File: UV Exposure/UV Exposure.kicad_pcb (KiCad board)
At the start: 2 copper layers, 90 x 90 mm, 90 parts

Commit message: PCB rearrange
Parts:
- moved D37 18.0 mm to (264.2, 38.1)
- moved D38 18.0 mm to (264.2, 50.5)
- moved D39 18.0 mm to (264.2, 63.5)
- moved D40 18.0 mm to (264.2, 76.2)
- moved D41 18.0 mm to (264.2, 88.9)
- moved D42 18.0 mm to (264.2, 101.6)
- moved D31 15.5 mm to (251.5, 38.1)
- moved D32 15.5 mm to (251.5, 50.8)
- moved D33 15.5 mm to (251.5, 63.5)
- moved D36 15.5 mm to (251.5, 101.6)
- moved D34 15.5 mm to (251.5, 76.2)
- moved D35 15.5 mm to (251.5, 88.9)
- moved D26 13.0 mm to (238.8, 50.8)
- moved D27 13.0 mm to (238.8, 63.5)
- moved D30 13.0 mm to (238.8, 101.6)
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
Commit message: Reposition SMD Resistor
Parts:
- moved R35 185.6 mm to (314.9, 108.4)
- moved R33 167.0 mm to (299.9, 108.4)
- moved R36 165.0 mm to (314.9, 111.0)
- moved R26 162.6 mm to (258.0, 111.1)
- moved R34 156.5 mm to (300.0, 111.0)
- moved R32 147.3 mm to (275.1, 111.0)
- moved R15 138.5 mm to (229.3, 108.4)
- moved R31 135.6 mm to (275.1, 108.4)
- moved R30 129.0 mm to (269.7, 111.0)
- moved R28 127.6 mm to (264.2, 111.0)
- moved R29 125.4 mm to (269.7, 108.4)
- moved R27 125.3 mm to (264.2, 108.4)
- moved R25 124.6 mm to (258.0, 108.4)
- moved R19 121.7 mm to (240.7, 108.4)
- moved R4 118.1 mm to (193.8, 111.0)
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
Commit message: Rearrange components
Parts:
- moved D43 165.2 mm to (134.6, 38.1)
- moved D44 165.2 mm to (134.6, 50.8)
- moved D45 165.2 mm to (134.6, 63.5)
- moved D46 165.2 mm to (134.6, 76.2)
- moved D47 165.2 mm to (134.6, 88.9)
- moved D48 165.2 mm to (134.6, 101.6)
- moved D37 142.3 mm to (121.9, 38.1)
- moved D38 142.3 mm to (121.9, 50.5)
- moved D39 142.3 mm to (121.9, 63.5)
- moved D40 142.3 mm to (121.9, 76.2)
- moved D41 142.3 mm to (121.9, 88.9)
- moved D42 142.3 mm to (121.9, 101.6)
- moved D1 142.3 mm to (45.7, 38.1)
- moved D2 142.3 mm to (45.7, 50.8)
- moved D3 142.3 mm to (45.7, 63.5)
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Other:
- board size 90 x 90 mm -> 102 x 90 mm

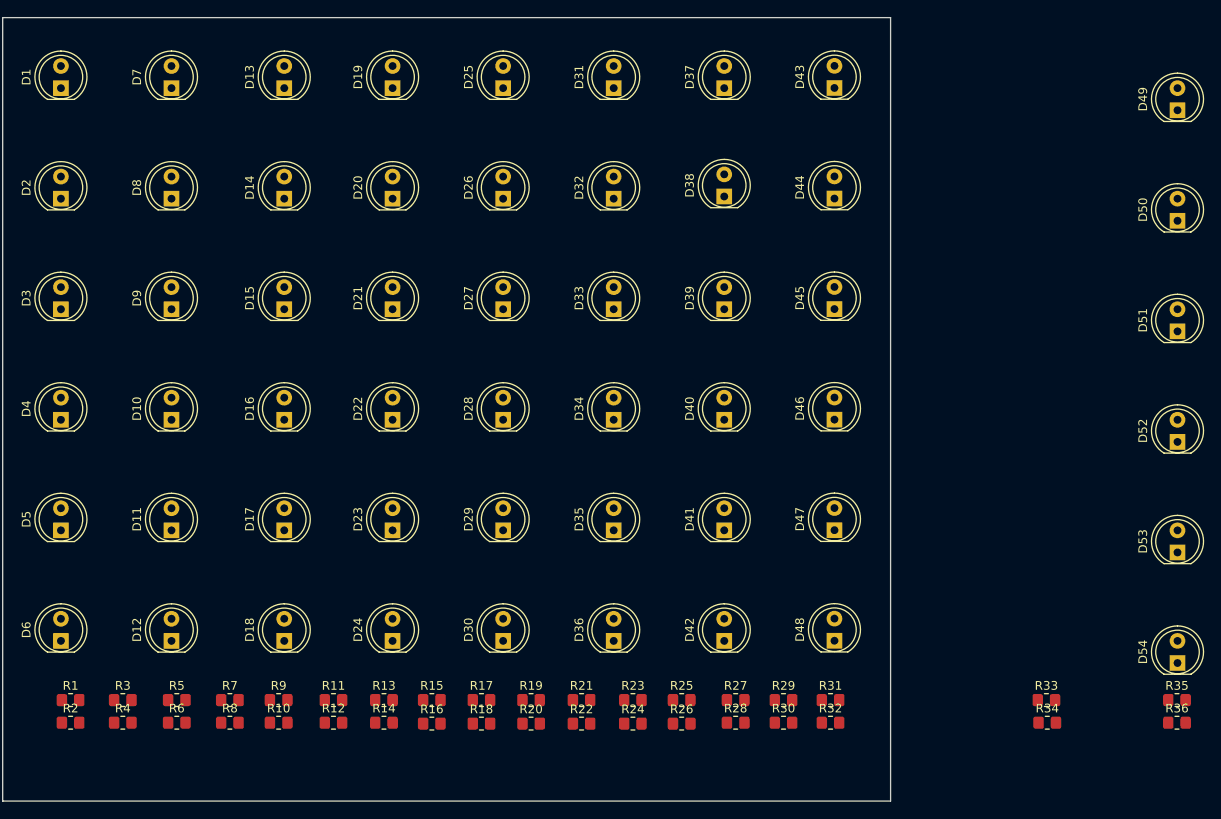
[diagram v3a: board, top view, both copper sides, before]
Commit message: drawing pcb track
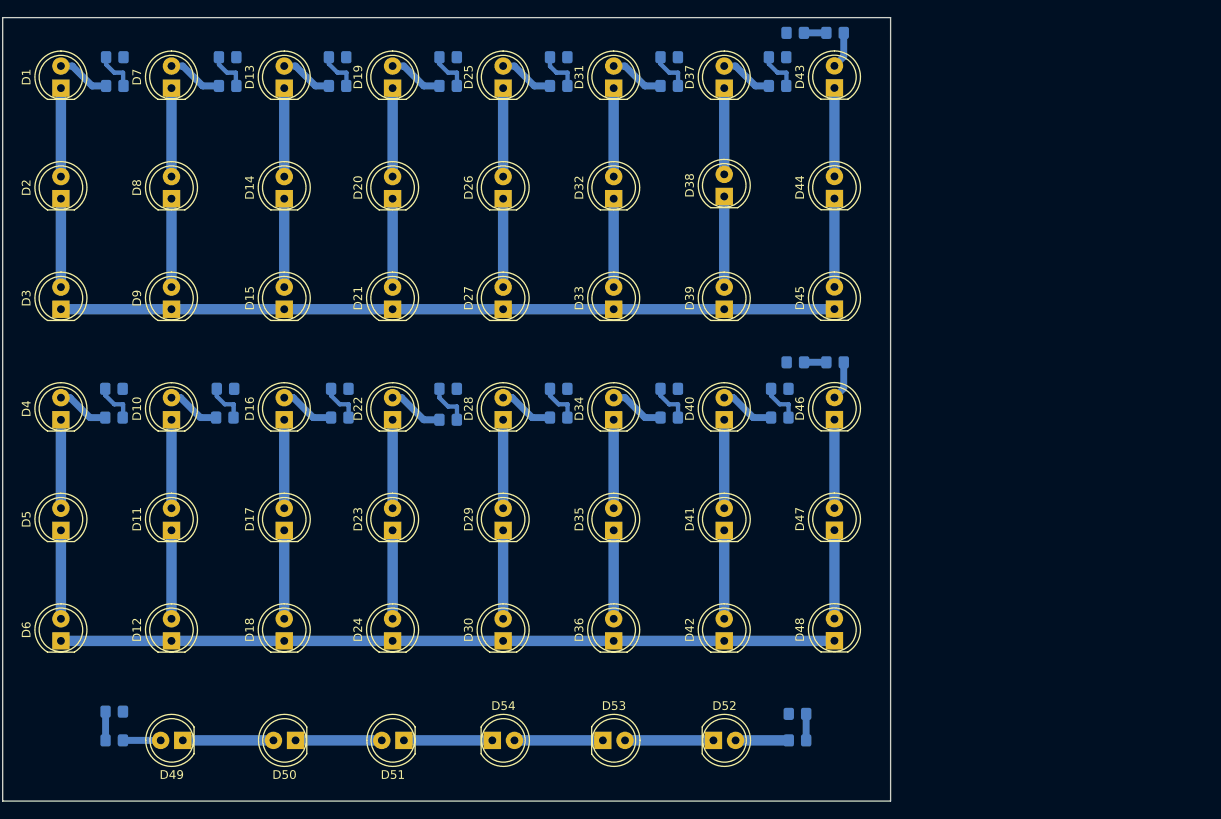
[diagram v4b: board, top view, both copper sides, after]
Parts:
- R1, R10, R11, R12, R13, R14, R15, R16, R17, R18, R19, R2, R20, R21, R22, R23, R24, R25, R26, R27, R28, R29, R3, R30, R31, R32, R33, R34, R35, R36, R4, R5, R6, R7, R8, R9: moved to B.Cu
- moved D49 135.3 mm to (59.7, 113.0), turned to 180 degrees
- moved D50 117.6 mm to (72.6, 113.0), turned to 180 degrees
- moved R34 107.2 mm to (51.8, 113.0), turned to 180 degrees
- moved R33 107.1 mm to (51.8, 109.7)
- moved D51 100.5 mm to (85.1, 113.0), turned to 180 degrees
- moved R30 79.5 mm to (134.6, 31.8), turned to 180 degrees
- moved D54 79.2 mm to (95.2, 113.0), turned to 0 degrees
- moved R29 76.7 mm to (130.0, 31.8), turned to 180 degrees
- moved R25 74.7 mm to (128.0, 34.5)
- moved R21 74.5 mm to (115.6, 34.5)
- moved R17 74.4 mm to (102.9, 34.5)
- moved R13 74.2 mm to (90.2, 34.5)
- moved R9 74.2 mm to (77.5, 34.5)
- moved R5 74.1 mm to (64.8, 34.5)
- moved R26 74.1 mm to (128.0, 37.8)
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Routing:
- net GND: track 0.00 -> 188.2 mm
- net Net-(D49-Pad1): track 0.00 -> 10.4 mm
- net Net-(D38-Pad1): track 0.00 -> 10.4 mm
- net Net-(D52-Pad1): track 0.00 -> 10.2 mm
- net Net-(D8-Pad1): track 0.00 -> 10.2 mm
- net Net-(D44-Pad1): track 0.00 -> 10.2 mm
- net Net-(D32-Pad1): track 0.00 -> 10.2 mm
- net Net-(D26-Pad1): track 0.00 -> 10.2 mm
- net Net-(D20-Pad1): track 0.00 -> 10.2 mm
- net Net-(D2-Pad1): track 0.00 -> 10.2 mm
- net Net-(D14-Pad1): track 0.00 -> 10.2 mm
- net Net-(D7-Pad1): track 0.00 -> 10.2 mm
- net Net-(D53-Pad1): track 0.00 -> 10.2 mm
- net Net-(D5-Pad1): track 0.00 -> 10.2 mm
- net Net-(D47-Pad1): track 0.00 -> 10.2 mm
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
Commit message: Add spacer drill hole
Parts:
- added P1: Conn_01x01, Connector_Pin:Pin_D1.0mm_L10.0mm, F.Cu at (45.7, 112.8)
- added P2: Conn_01x01, Connector_Pin:Pin_D1.0mm_L10.0mm, F.Cu at (134.6, 112.8)
- moved R35 12.9 mm to (117.6, 108.0)
- moved R33 10.8 mm to (62.5, 108.0)
- moved R36 9.58 mm to (122.2, 108.0), turned to 180 degrees
- moved R34 8.13 mm to (58.2, 108.0), turned to 0 degrees
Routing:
- net Net-(D52-Pad2): track 6.11 -> 5.09 mm
- net Net-(R33-Pad1): track 3.30 -> 2.32 mm
- net Net-(D49-Pad2): track 4.33 -> 5.09 mm
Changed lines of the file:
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@@
-(kicad_pcb (version 20171130) (host pcbnew "(5.1.9)-1")
+(kicad_pcb (version 20171130) (host pcbnew "(5.1.2)-1")
   (general
     (thickness 1.6)
     (drawings 6)
-    (tracks 176)
+    (tracks 178)
     (zones 0)
-    (modules 90)
-    (nets 75)
+    (modules 92)
+    (nets 77)
   )
   (page A4)
@@
   )
   (setup
-    (last_trace_width 1.2)
+    (last_trace_width 0.8)
     (user_trace_width 0.5)
     (user_trace_width 0.8)
@@
     (mod_text_size 1 1)
     (mod_text_width 0.15)
-    (pad_size 2 2)
-    (pad_drill 0.9)
+    (pad_size 4.064 4.064)
+    (pad_drill 3.048)
     (pad_to_mask_clearance 0)
     (aux_axis_origin 0 0)
@@
   (net 73 "Net-(R33-Pad1)")
   (net 74 "Net-(R35-Pad1)")
+  (net 75 "Net-(P1-Pad1)")
+  (net 76 "Net-(P2-Pad1)")
   (net_class Default "This is the default net class."
     (clearance 0.2)
@@
     (add_net "Net-(D7-Pad2)")
     (add_net "Net-(D8-Pad1)")
+    (add_net "Net-(P1-Pad1)")
+    (add_net "Net-(P2-Pad1)")
     (add_net "Net-(R1-Pad1)")
     (add_net "Net-(R10-Pad2)")
@@
     (add_net "Net-(R7-Pad1)")
   )
+  (module Connector_Pin:Pin_D1.0mm_L10.0mm (layer F.Cu)
+    (at 134.62 112.777001)
+    (descr "solder Pin_ diameter 1.0mm, hole diameter 1.0mm (press fit), length 10.0mm")
+    (tags "solder Pin_ press fit")
+    (fp_text reference P2 (at 0 -3.303001) (layer F.SilkS)
+      (effects (font (size 1 1) (thickness 0.15)))
+    )
+    (fp_text value Conn_01x01 (at 0 3.808999) (layer F.Fab)
+      (effects (font (size 1 1) (thickness 0.15)))
+    )
+    (fp_circle (center 0 0) (end 2.54 0.05) (layer F.SilkS) (width 0.12))
+    (fp_circle (center 0 0) (end 1 0) (layer F.Fab) (width 0.12))
+    (fp_circle (center 0 0) (end 0.5 0) (layer F.Fab) (width 0.12))
+    (fp_circle (center 0 0) (end 1.5 0) (layer F.CrtYd) (width 0.05))
+    (fp_text user %R (at 0 -3.303001) (layer F.Fab)
+      (effects (font (size 1 1) (thickness 0.15)))
+    )
+    (pad 1 thru_hole circle (at 0 0) (size 4.064 4.064) (drill 3.048) (layers *.Cu *.Mask)
+      (net 76 "Net-(P2-Pad1)"))
+  )
+  (module Connector_Pin:Pin_D1.0mm_L10.0mm (layer F.Cu)
+    (at 45.72 112.776)
+    (descr "solder Pin_ diameter 1.0mm, hole diameter 1.0mm (press fit), length 10.0mm")
+    (tags "solder Pin_ press fit")
+    (fp_text reference P1 (at 0 -3.81) (layer F.SilkS)
+      (effects (font (size 1 1) (thickness 0.15)))
+    )
+    (fp_text value Conn_01x01 (at 0 3.556) (layer F.Fab) hide
+      (effects (font (size 1 1) (thickness 0.15)))
+    )
+    (fp_text user %R (at 0 -3.81) (layer F.Fab) hide
+      (effects (font (size 1 1) (thickness 0.15)))
+    )
+    (fp_circle (center 0 0) (end 1.5 0) (layer F.CrtYd) (width 0.05))
+    (fp_circle (center 0 0) (end 0.5 0) (layer F.Fab) (width 0.12))
+    (fp_circle (center 0 0) (end 1 0) (layer F.Fab) (width 0.12))
+    (fp_circle (center 0 0) (end 2.54 0) (layer F.SilkS) (width 0.12))
+    (pad 1 thru_hole circle (at 0 0) (size 4.064 4.064) (drill 3.048) (layers *.Cu *.Mask)
+      (net 75 "Net-(P1-Pad1)"))
+  )
   (module LED_THT:LED_D5.0mm (layer F.Cu)
     (at 45.69 38.1 90)
@@
       (effects (font (size 1 1) (thickness 0.15)))
     )
-    (fp_text value LED (at 1.27 3.96) (layer F.Fab)
+    (fp_text value LED (at -3.81 -1.778) (layer F.Fab)
       (effects (font (size 1 1) (thickness 0.15)))
     )
@@
     (descr "LED, diameter 5.0mm, 2 pins, http://cdn-reichelt.de/documents/datenblatt/A500/LL-504BC2E-009.pdf")
     (tags "LED diameter 5.0mm 2 pins")
-    (fp_text reference D52 (at 1.27 -3.96) (layer F.SilkS)
+    (fp_text reference D52 (at -3.81 1.778) (layer F.SilkS)
       (effects (font (size 1 1) (thickness 0.15)))
     )
@@
   )
   (module Resistor_SMD:R_0805_2012Metric_Pad1.20x1.40mm_HandSolder (layer B.Cu)
-    (at 51.816 109.728)
+    (at 62.484 107.95)
     (descr "Resistor SMD 0805 (2012 Metric), square (rectangular) end terminal, IPC_7351 nominal with elongated pad for handsoldering. (Body size source: IPC-SM-782 page 72, https://www.pcb-3d.com/wordpress/wp-content/uploads/ipc-sm-782a_amendment_1_and_2.pdf), generated with kicad-footprint-generator")
     (tags "resistor handsolder")
@@
   )
   (module Resistor_SMD:R_0805_2012Metric_Pad1.20x1.40mm_HandSolder (layer B.Cu)
-    (at 51.816 113.03 180)
+    (at 58.166 107.95)
     (descr "Resistor SMD 0805 (2012 Metric), square (rectangular) end terminal, IPC_7351 nominal with elongated pad for handsoldering. (Body size source: IPC-SM-782 page 72, https://www.pcb-3d.com/wordpress/wp-content/uploads/ipc-sm-782a_amendment_1_and_2.pdf), generated with kicad-footprint-generator")
     (tags "resistor handsolder")
@@
       (effects (font (size 0.5 0.5) (thickness 0.08)) (justify mirror))
     )
-    (pad 2 smd roundrect (at 1 0 180) (size 1.2 1.4) (layers B.Cu B.Paste B.Mask) (roundrect_rratio 0.208333)
+    (pad 2 smd roundrect (at 1 0) (size 1.2 1.4) (layers B.Cu B.Paste B.Mask) (roundrect_rratio 0.208333)
       (net 73 "Net-(R33-Pad1)"))
-    (pad 1 smd roundrect (at -1 0 180) (size 1.2 1.4) (layers B.Cu B.Paste B.Mask) (roundrect_rratio 0.208333)
+    (pad 1 smd roundrect (at -1 0) (size 1.2 1.4) (layers B.Cu B.Paste B.Mask) (roundrect_rratio 0.208333)
       (net 51 "Net-(D49-Pad2)"))
     (model ${KISYS3DMOD}/Resistor_SMD.3dshapes/R_0805_2012Metric.wrl
@@
   )
   (module Resistor_SMD:R_0805_2012Metric_Pad1.20x1.40mm_HandSolder (layer B.Cu)
-    (at 130.302 109.982 180)
+    (at 117.602 107.95 180)
     (descr "Resistor SMD 0805 (2012 Metric), square (rectangular) end terminal, IPC_7351 nominal with elongated pad for handsoldering. (Body size source: IPC-SM-782 page 72, https://www.pcb-3d.com/wordpress/wp-content/uploads/ipc-sm-782a_amendment_1_and_2.pdf), generated with kicad-footprint-generator")
     (tags "resistor handsolder")
@@
   )
   (module Resistor_SMD:R_0805_2012Metric_Pad1.20x1.40mm_HandSolder (layer B.Cu)
-    (at 130.302 113.03)
+    (at 122.174 107.95 180)
     (descr "Resistor SMD 0805 (2012 Metric), square (rectangular) end terminal, IPC_7351 nominal with elongated pad for handsoldering. (Body size source: IPC-SM-782 page 72, https://www.pcb-3d.com/wordpress/wp-content/uploads/ipc-sm-782a_amendment_1_and_2.pdf), generated with kicad-footprint-generator")
     (tags "resistor handsolder")
@@
       (effects (font (size 0.5 0.5) (thickness 0.08)) (justify mirror))
     )
-    (pad 2 smd roundrect (at 1 0) (size 1.2 1.4) (layers B.Cu B.Paste B.Mask) (roundrect_rratio 0.208333)
+    (pad 2 smd roundrect (at 1 0 180) (size 1.2 1.4) (layers B.Cu B.Paste B.Mask) (roundrect_rratio 0.208333)
       (net 74 "Net-(R35-Pad1)"))
-    (pad 1 smd roundrect (at -1 0) (size 1.2 1.4) (layers B.Cu B.Paste B.Mask) (roundrect_rratio 0.208333)
+    (pad 1 smd roundrect (at -1 0 180) (size 1.2 1.4) (layers B.Cu B.Paste B.Mask) (roundrect_rratio 0.208333)
       (net 54 "Net-(D52-Pad2)"))
     (model ${KISYS3DMOD}/Resistor_SMD.3dshapes/R_0805_2012Metric.wrl
@@
   (segment (start 134.55 88.882) (end 134.55 99.042) (width 1.2) (layer B.Cu) (net 49))
   (segment (start 59.69 113.03) (end 70.104 113.03) (width 1.2) (layer B.Cu) (net 50))
-  (segment (start 52.816 113.03) (end 57.15 113.03) (width 0.8) (layer B.Cu) (net 51))
+  (segment (start 57.166 113.014) (end 57.15 113.03) (width 0.8) (layer B.Cu) (net 51))
+  (segment (start 57.166 107.95) (end 57.166 113.014) (width 0.8) (layer B.Cu) (net 51))
   (segment (start 72.644 113.03) (end 82.55 113.03) (width 1.2) (layer B.Cu) (net 52))
   (segment (start 110.49 113.03) (end 120.65 113.03) (width 1.2) (layer B.Cu) (net 53))
-  (segment (start 123.19 113.03) (end 129.302 113.03) (width 1.2) (layer B.Cu) (net 54))
+  (segment (start 123.174 113.014) (end 123.19 113.03) (width 0.8) (layer B.Cu) (net 54))
+  (segment (start 123.174 107.95) (end 123.174 113.014) (width 0.8) (layer B.Cu) (net 54))
   (segment (start 97.79 113.03) (end 107.95 113.03) (width 1.2) (layer B.Cu) (net 55))
   (segment (start 50.88 34.544) (end 50.88 35.386) (width 0.5) (layer B.Cu) (net 57))
@@
   (segment (start 131.048 31.75) (end 133.62 31.75) (width 0.8) (layer B.Cu) (net 71))
   (segment (start 131.064 69.596) (end 133.62 69.596) (width 0.8) (layer B.Cu) (net 72))
-  (segment (start 50.816 109.728) (end 50.816 113.03) (width 0.8) (layer B.Cu) (net 73))
-  (segment (start 131.302 109.982) (end 131.302 113.03) (width 0.8) (layer B.Cu) (net 74))
+  (segment (start 59.166 107.95) (end 61.484 107.95) (width 0.8) (layer B.Cu) (net 73))
+  (segment (start 118.602 107.95) (end 121.174 107.95) (width 0.8) (layer B.Cu) (net 74))
 )

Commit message: Update PCB track
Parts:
- added REF**: Pin_D1.0mm_L10.0mm, Connector_Pin:Pin_D1.0mm_L10.0mm, F.Cu at (128.5, 109.0)
- added REF**: Pin_D1.0mm_L10.0mm, Connector_Pin:Pin_D1.0mm_L10.0mm, F.Cu at (52.1, 109.2)
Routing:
- net +12V: track 0.00 -> 376.1 mm
- added copper zone on B.Cu, net +12V
- added copper zone on B.Cu, net GND
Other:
- board text added: "UV Exposure Light"
